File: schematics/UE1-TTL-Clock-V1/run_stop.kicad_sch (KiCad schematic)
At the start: 17 parts, among them SW1 RUN, SW2 HALT, SW3 RESET, U1 74LS74, U5 74LS132, U6 74LS02

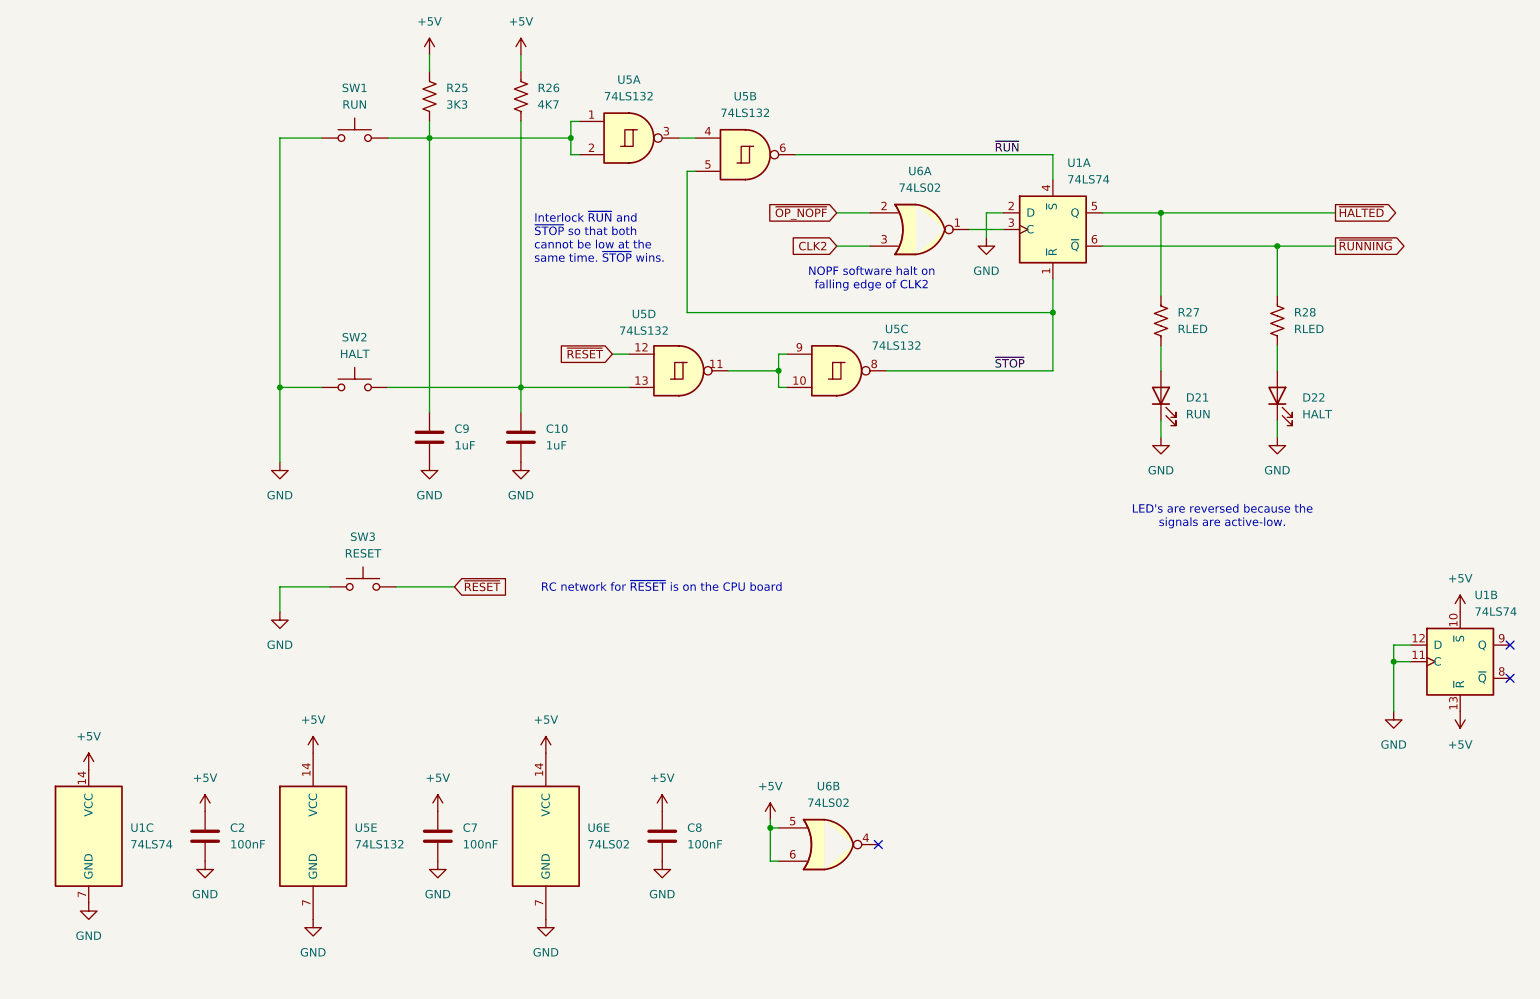
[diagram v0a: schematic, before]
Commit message: Update the clock schematic with V2 modifications
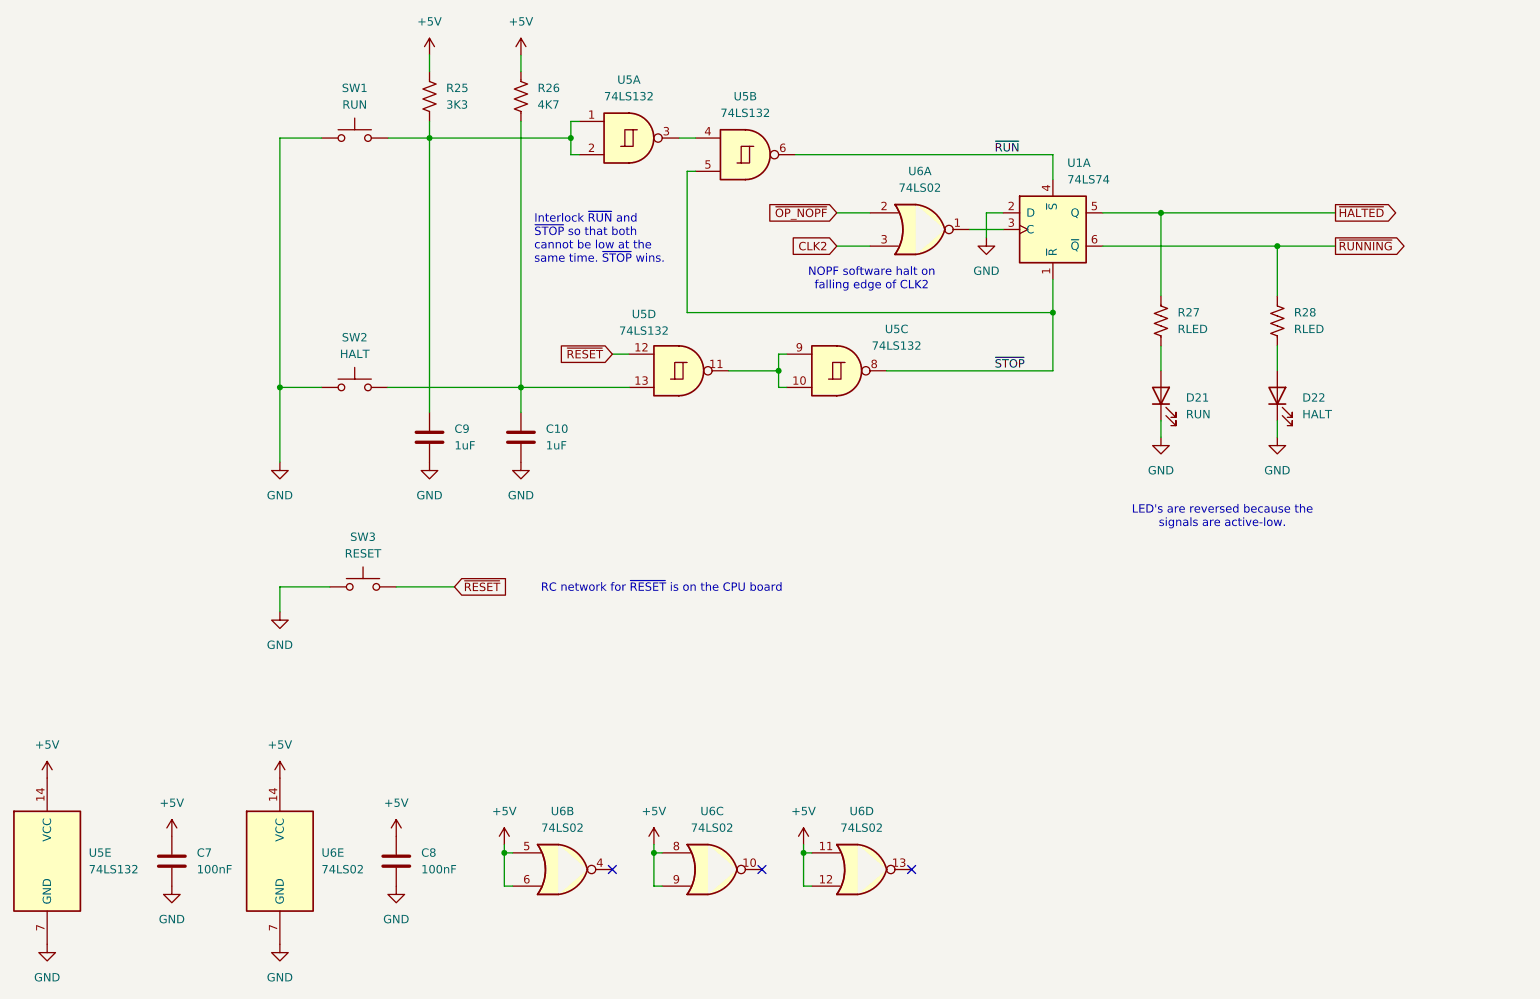
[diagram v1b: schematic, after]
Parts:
- removed C2: 100nF, Capacitor_THT:C_Disc_D5.0mm_W2.5mm_P5.00mm, symbol Device:C
- removed unit 2 of U1
- removed unit 3 of U1
- added unit 3 of U6
- added unit 4 of U6
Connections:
- net +5V: now also U6.11, U6.12, U6.8, U6.9
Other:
- moved on the sheet: C7, C8, U5E, U6B, U6E
